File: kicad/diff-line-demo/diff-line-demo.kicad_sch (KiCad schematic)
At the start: 0 parts

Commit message: HDMI connectors selection, begin of PCB.
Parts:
- added J1, J2: HDMI_A, Connector_Video:HDMI_A_Amphenol_10029449-x01xLF_Horizontal, symbol Connector:HDMI_A
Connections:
- new net: J1.1 (D2+), J2.1 (D2+)
- new net: J1.3 (D2-), J2.3 (D2-)
- new net: J1.4 (D1+), J2.4 (D1+)
- new net: J1.6 (D1-), J2.6 (D1-)
- new net: J1.7 (D0+), J2.7 (D0+)
- new net: J1.9 (D0-), J2.9 (D0-)

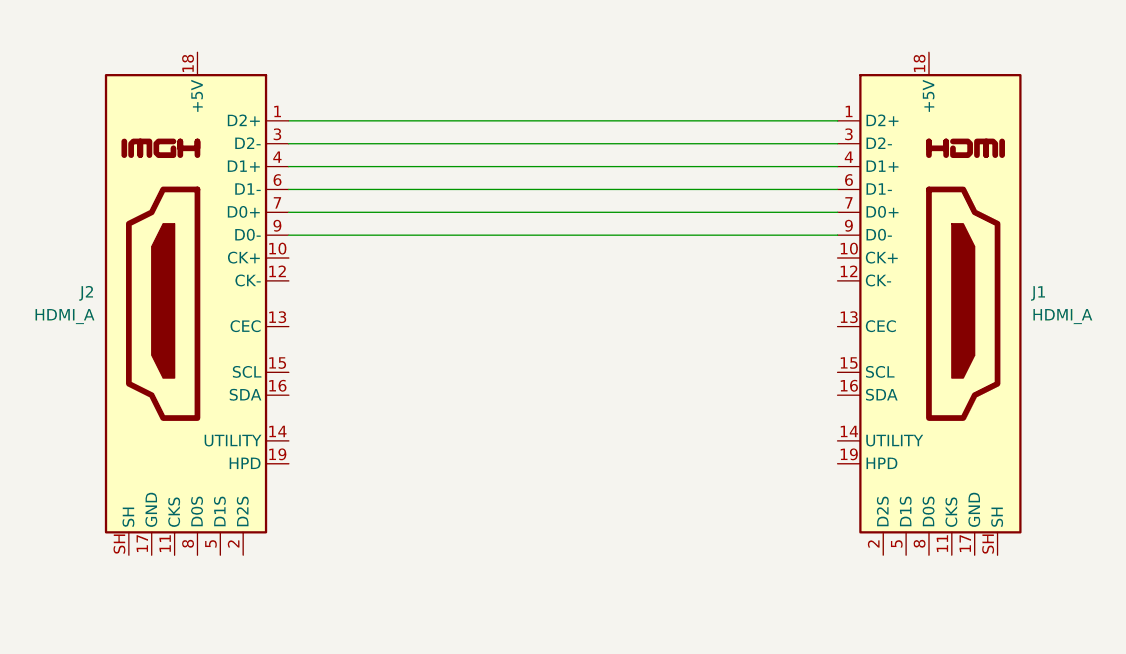
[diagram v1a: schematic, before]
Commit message: Route all signals.
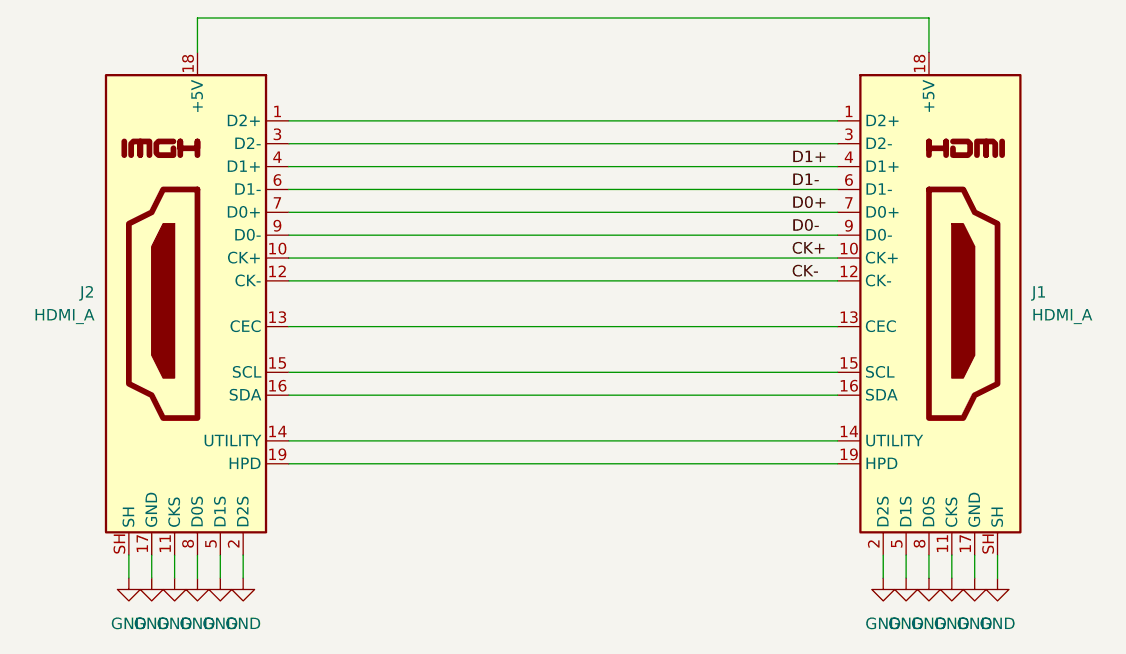
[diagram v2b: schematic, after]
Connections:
- net CK+: now reaches J1.10 (CK+)
- net CK+: now also J2.10 (CK+)
- net GND: now reaches J1.11 (CKS)
- net GND: now also J1.17 (GND), J1.2 (D2S), J1.5 (D1S), J1.8 (D0S), J1.SH, J2.11 (CKS), J2.17 (GND), J2.2 (D2S), J2.5 (D1S), J2.8 (D0S), J2.SH
- net CK-: now reaches J1.12 (CK-)
- net CK-: now also J2.12 (CK-)
- net at J1.13 (CEC): now also J2.13 (CEC)
- net at J1.14 (UTILITY): now also J2.14 (UTILITY)
- net at J1.15 (SCL): now also J2.15 (SCL)
- net at J1.16 (SDA): now also J2.16 (SDA)
- net at J1.18 (+5V): now also J2.18 (+5V)
- net at J1.19 (HPD): now also J2.19 (HPD)
- net D1+: now reaches J1.4 (D1+), J2.4 (D1+)
- net D1-: now reaches J1.6 (D1-), J2.6 (D1-)
- net D0+: now reaches J1.7 (D0+), J2.7 (D0+)
- net D0-: now reaches J1.9 (D0-), J2.9 (D0-)
